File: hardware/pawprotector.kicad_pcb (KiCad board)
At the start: 2 copper layers, 32.5 x 16.6 mm, 25 parts, among them J1 USB_A, J2 USB_A, U1 TPS2514A, U2 TPD2E001, U3 TPS2561

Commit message: Usb-c
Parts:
- removed C1: 150uF, Capacitor_SMD:CP_Elec_6.3x5.4
- removed C2: 0.22uF, Capacitor_SMD:C_0402_1005Metric
- removed C3, C5, C6: 0.1uF, Capacitor_SMD:C_0402_1005Metric
- removed C4: 10uF, Capacitor_SMD:C_0805_2012Metric
- removed D1: ON, LED_SMD:LED_0402_1005Metric
- removed J1: USB_A, usbCondom:C46394
- removed J2: USB_A, usbCondom:875832010BLF
- removed R1: 43.2K, Resistor_SMD:R_0402_1005Metric
- removed R2, R4: 49.9K, Resistor_SMD:R_0402_1005Metric
- removed R3: 75K, Resistor_SMD:R_0402_1005Metric
- removed R5: 20K, Resistor_SMD:R_0402_1005Metric
- removed R6: 100K, Resistor_SMD:R_0402_1005Metric
- removed R7: 1K, Resistor_SMD:R_0402_1005Metric
- removed U1: TPS2514A, Package_TO_SOT_SMD:SOT-23-6
- removed U2: TPD2E001, Package_TO_SOT_SMD:SOT-553
- removed U3: TPS2561, Package_SON:VSON-10-1EP_3x3mm_P0.5mm_EP1.65x2.4mm_ThermalVias
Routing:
- net /FAULT: track 41.2 -> 0.00 mm, vias 2 -> 0
- net +5V: track 39.4 -> 0.00 mm, vias 4 -> 0
- net VBUS: track 22.6 -> 0.00 mm, vias 2 -> 0
- net GND: track 21.8 -> 0.00 mm, vias 7 -> 0
- net /D-: track 14.1 -> 0.00 mm, vias 1 -> 0
- net /D+: track 12.0 -> 0.00 mm, vias 1 -> 0
- net /DCP-: track 8.41 -> 0.00 mm
- net /DCP+: track 3.76 -> 0.00 mm
- net Net-(U3-ILM): track 1.83 -> 0.00 mm
- net Net-(D1-K): track 1.43 -> 0.00 mm

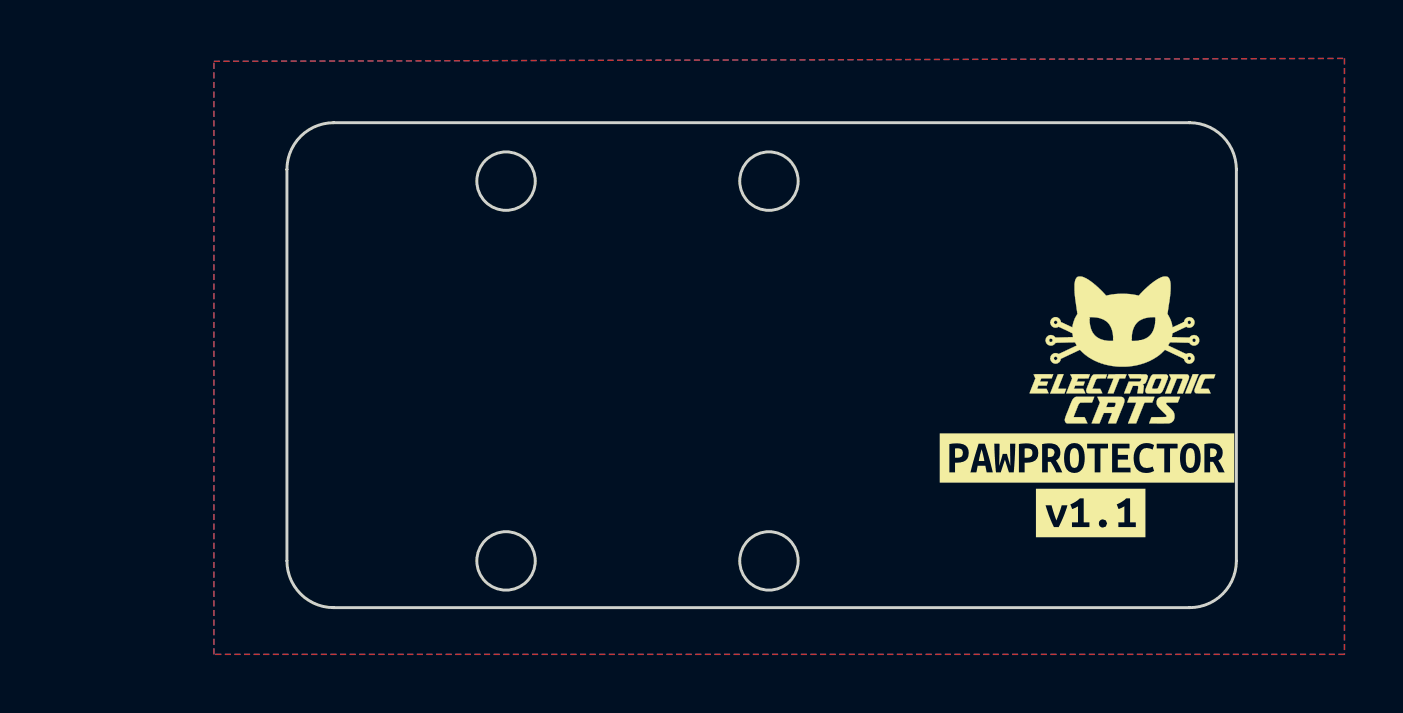
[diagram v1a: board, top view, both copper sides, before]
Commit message: Ruteo PCB
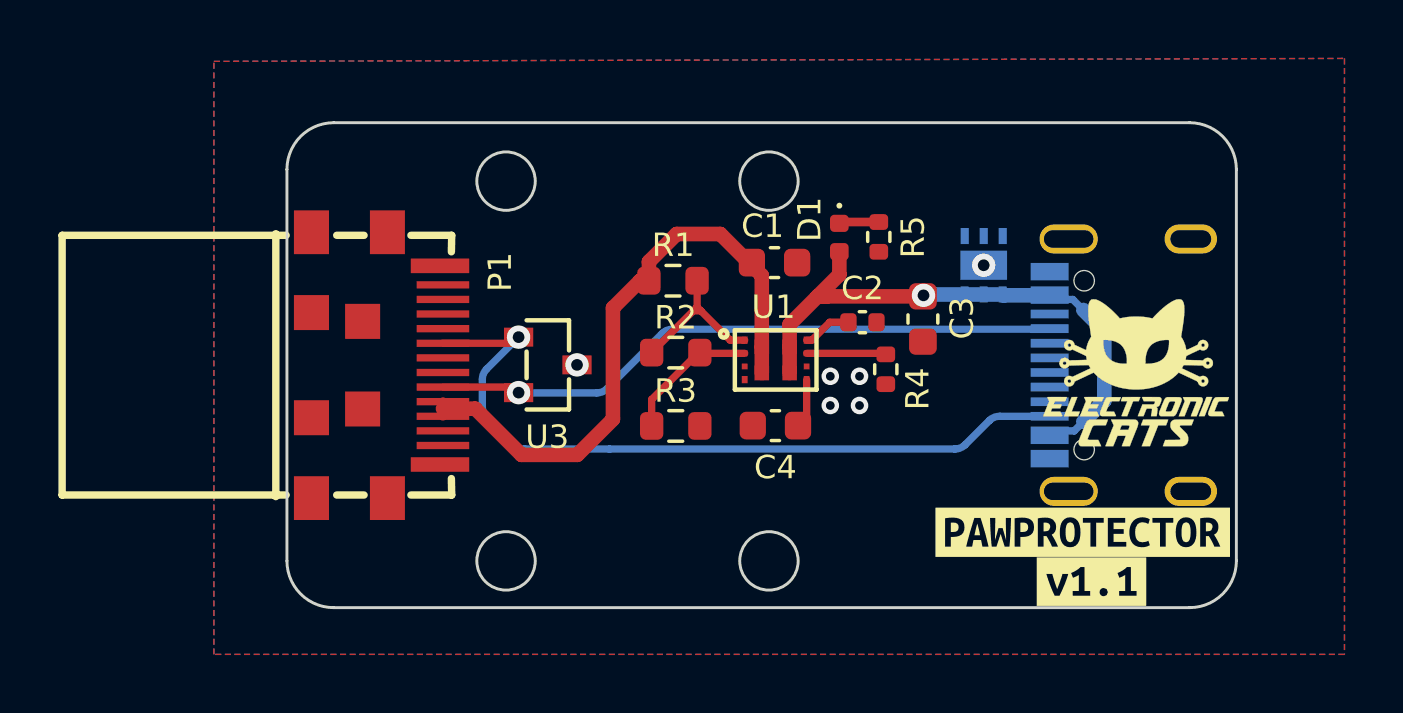
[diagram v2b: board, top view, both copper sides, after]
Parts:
- added C1: 1uF, Capacitor_SMD:C_0603_1608Metric, F.Cu at (144.0, 90.3)
- added C2: 12nF, Capacitor_SMD:C_0402_1005Metric, F.Cu at (147.0, 92.4)
- added C3: 4.7uF, Capacitor_SMD:C_0603_1608Metric, F.Cu at (149.1, 92.3)
- added C4: 10nF, Capacitor_SMD:C_0603_1608Metric, F.Cu at (144.0, 95.9)
- added D1: ON, LED_SMD:LED_0402_1005Metric, F.Cu at (146.2, 89.5)
- added J1: USB_C_Receptacle, USB-C-FEMALE:USB-C-SMD_KH-TYPE-C-16P, B.Cu at (155.8, 93.8)
- added P1: USB_C_Plug, USB-C_Male:USB-C-SMD_TYPE-C-31-G-10, F.Cu at (130.4, 93.8)
- added R1: 75k, Resistor_SMD:R_0603_1608Metric, F.Cu at (140.5, 91.0)
- added R2: 20.5k, Resistor_SMD:R_0603_1608Metric, F.Cu at (140.6, 93.4)
- added R3: 5k, Resistor_SMD:R_0603_1608Metric, F.Cu at (140.6, 95.9)
- added R4: 953, Resistor_SMD:R_0402_1005Metric, F.Cu at (147.8, 94.0)
- added R5: 1k, Resistor_SMD:R_0402_1005Metric, F.Cu at (147.6, 89.5)
- added U1: TPS259480AYWPR, TPS259480:POWERWCSP-12_L2.5-W1.7_TPS259482AYWPR, F.Cu at (144.0, 93.7)
- added U2: TVS2200DRVR(ES), TVS2200DRVR:DFN-6_L2.0-W2.0-P0.65-BL-EP1.6, B.Cu at (151.1, 90.4)
- added U3: ESD752DBZR, ESD752DBZR:SOT-23-3_L2.9-W1.3-P1.90-LS2.4-BR, F.Cu at (136.2, 93.8)
- moved kibuzzard-65CAA4BB 2.55 mm to (154.5, 99.6)
- moved kibuzzard-65CAA533 2.35 mm to (154.8, 101.3)
- moved G*** 0.91 mm to (156.4, 94.1)
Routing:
- net /CC2: track 0.00 -> 26.4 mm, vias 0 -> 1
- net +5V: track 0.00 -> 21.8 mm
- net /CC1: track 0.00 -> 21.6 mm, vias 0 -> 1
- net VBUS: track 0.00 -> 20.1 mm, vias 0 -> 1
- net /UVLO: track 0.00 -> 5.58 mm
- net /OVLO: track 0.00 -> 4.79 mm
- net Net-(U1-ILM): track 0.00 -> 2.87 mm
- net Net-(U1-DVDT): track 0.00 -> 1.70 mm
- net /ITIMER: track 0.00 -> 1.68 mm
- net Net-(D1-K): track 0.00 -> 1.37 mm
- net GND: vias 0 -> 6

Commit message: fix(pcb): optimizar espacio de componentes y agregar planos de voltaje
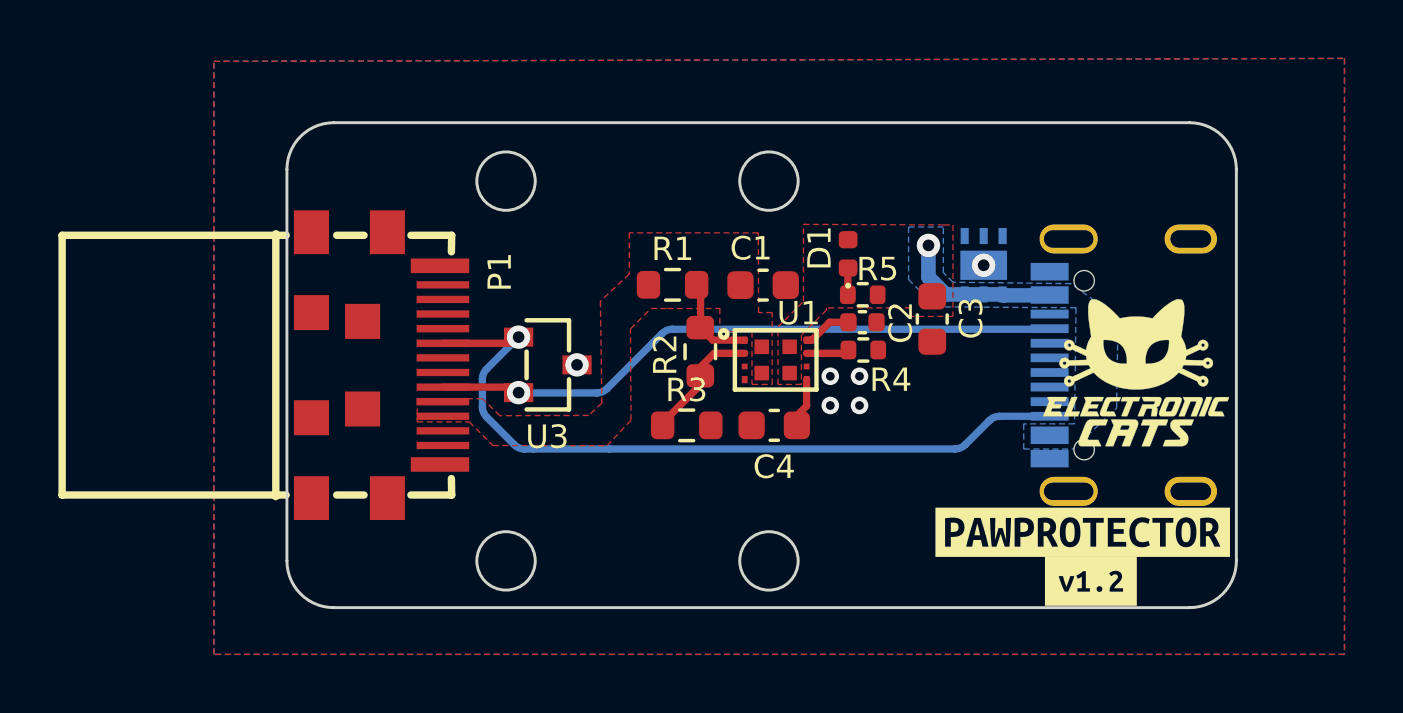
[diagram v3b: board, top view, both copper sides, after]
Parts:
- removed kibuzzard-65CAA533: G***, kibuzzard-65CAA533
- added kibuzzard-6AC40DF5: G***, kibuzzard-6AC40DF5, F.Cu at (154.8, 101.2)
- moved R5 2.05 mm to (147.0, 91.4), turned to 0 degrees
- moved R4 1.01 mm to (147.0, 93.3), turned to 0 degrees
- moved C1 0.86 mm to (143.6, 91.1)
- moved R2 0.84 mm to (141.4, 93.4), turned to -90 degrees
- moved D1 0.64 mm to (146.5, 90.0), turned to 90 degrees
- moved R3 0.38 mm to (141.0, 95.9)
- moved C3 0.32 mm to (149.4, 92.3)
- moved R1 0.14 mm to (140.5, 91.1)
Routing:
- net +5V: track 21.8 -> 0.13 mm
- net VBUS: track 20.1 -> 5.81 mm
- net /UVLO: track 5.58 -> 3.37 mm
- net Net-(U1-ILM): track 2.87 -> 1.50 mm
- added copper zone on F.Cu, net +5V
- added copper zone on B.Cu, net VBUS
- added copper zone on F.Cu, net VBUS

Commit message: feat(pcb): finalizar ruteo de componentes y planos GND y voltaje
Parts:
- removed kibuzzard-65CAA527: G***, kibuzzard-65CAA527
- added kibuzzard-6AC515D0: G***, kibuzzard-6AC515D0, B.Cu at (133.6, 93.5)
- C3: footprint Capacitor_SMD:C_0603_1608Metric -> Capacitor_SMD:C_0805_2012Metric
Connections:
- P1 pad 2: (no net) -> GND
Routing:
- net VBUS: track 5.81 -> 0.34 mm
